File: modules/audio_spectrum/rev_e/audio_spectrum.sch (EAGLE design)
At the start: 109 parts, among them J1 AUDIO-JACK-VERTICAL, J2 MODULE_GENERIC_DEBUG, J3 TC2030-JLINK-L, P1 4k-200k, P2 4k-200k, Q1 NX3008PBK, Q2 NX3008PBK, U1 AT45DB641EUDFN, U10 TLV62130, U2 MP23AB02B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

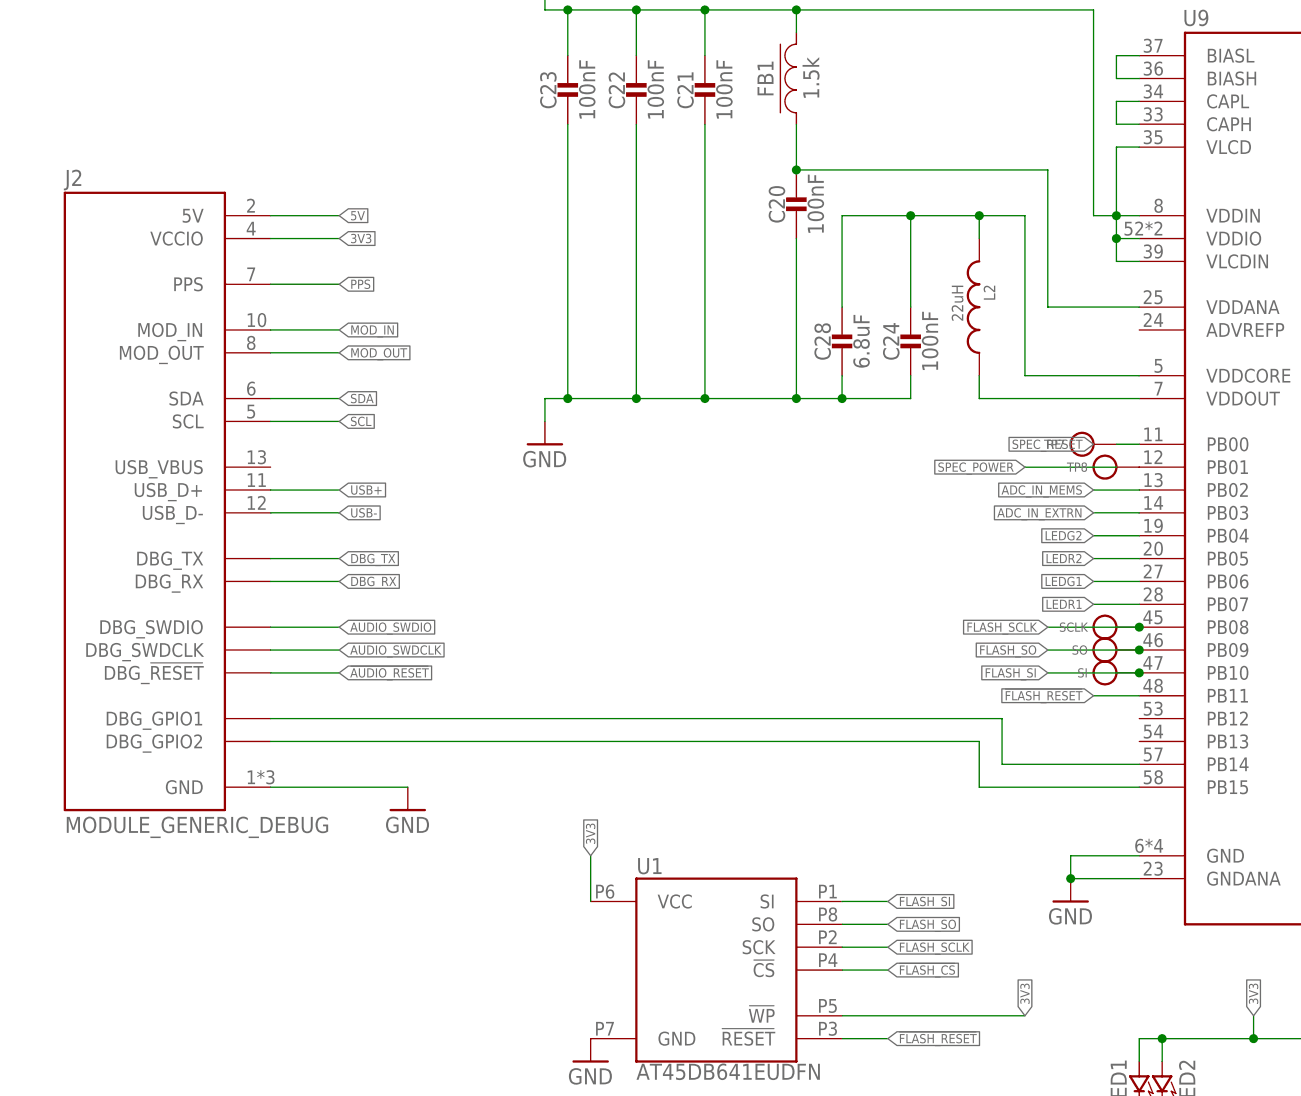
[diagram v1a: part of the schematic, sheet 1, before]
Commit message: changed to design block for header parts
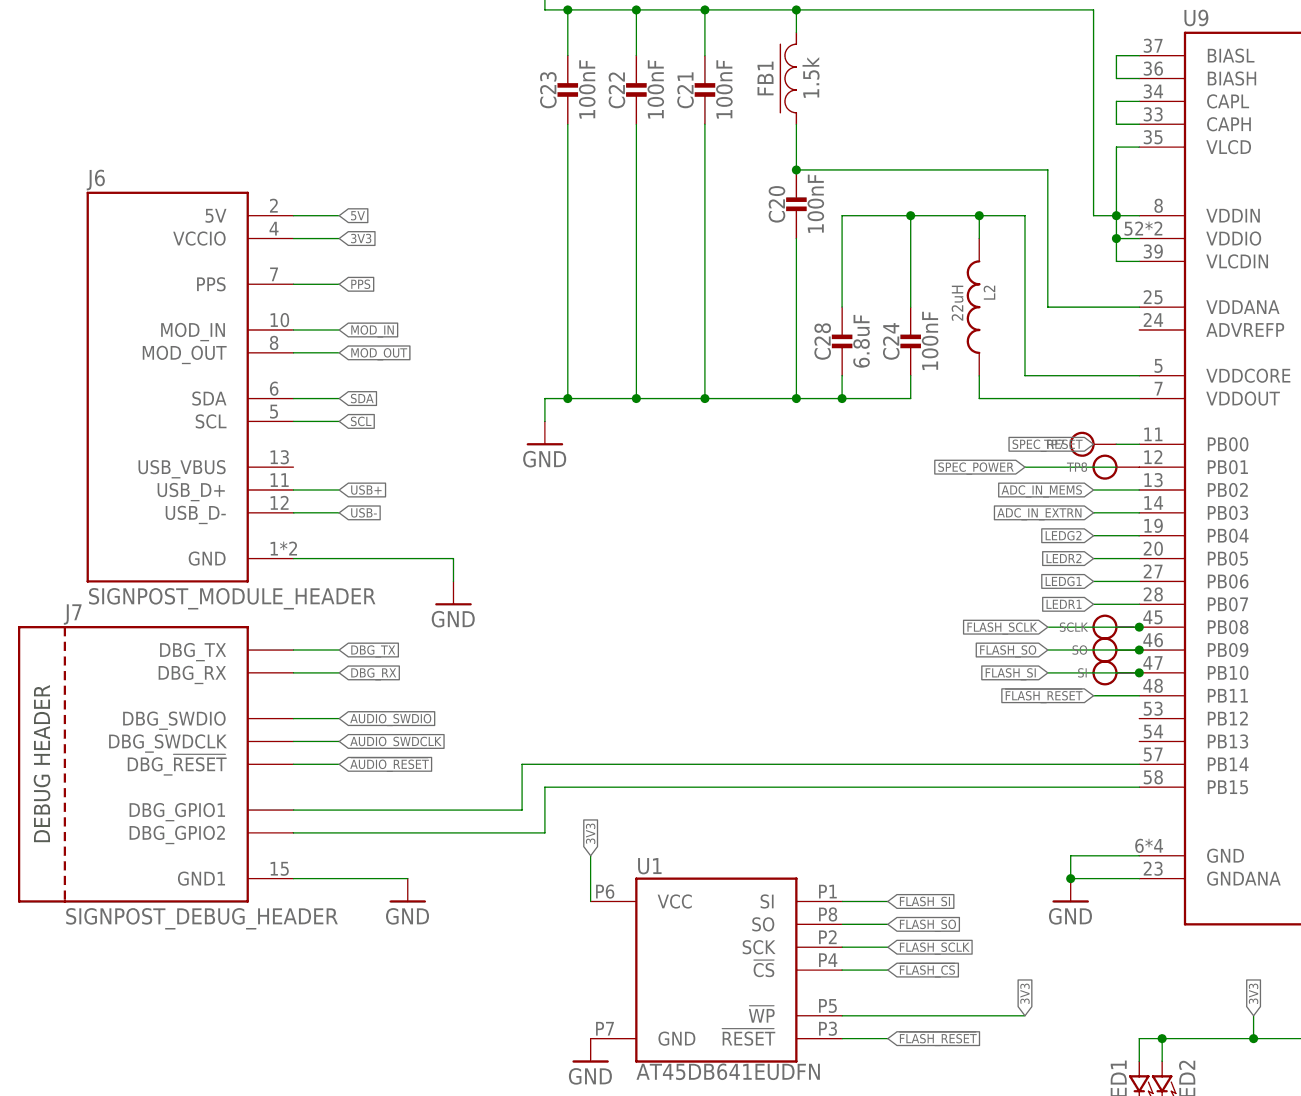
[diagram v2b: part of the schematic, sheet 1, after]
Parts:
- removed J2: MODULE_GENERIC_DEBUG, signpost:MODULE_GENERIC_DEBUG
- added J6: SIGNPOST_MODULE_HEADER, signpost:SIGNPOST_MODULE_HEADER
- added J7: SIGNPOST_DEBUG_HEADER, signpost:SIGNPOST_DEBUG_HEADER
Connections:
- net !AUDIO_RESET: now also J7.DBG_!RESET; no longer J2.DBG_!RESET
- net 3V3: now also J6.VCCIO; no longer J2.VCCIO
- net 5V: now also J6.5V; no longer J2.5V
- net AUDIO_SWDCLK: now also J7.DBG_SWDCLK; no longer J2.DBG_SWDCLK
- net AUDIO_SWDIO: now also J7.DBG_SWDIO; no longer J2.DBG_SWDIO
- net DBG_GPIO1: now also J7.DBG_GPIO1; no longer J2.DBG_GPIO1
- net DBG_GPIO2: now also J7.DBG_GPIO2; no longer J2.DBG_GPIO2
- net DBG_RX: now also J7.DBG_RX; no longer J2.DBG_RX
- net DBG_TX: now also J7.DBG_TX; no longer J2.DBG_TX
- net GND: now also J6.GND, J7.GND1; no longer J2.GND
- net MOD_IN: now also J6.MOD_IN; no longer J2.MOD_IN
- net MOD_OUT: now also J6.MOD_OUT; no longer J2.MOD_OUT
- net PPS: now also J6.PPS; no longer J2.PPS
- net SCL: now also J6.SCL; no longer J2.SCL
- net SDA: now also J6.SDA; no longer J2.SDA
- net USB+: now also J6.USB_D+; no longer J2.USB_D+
- net USB-: now also J6.USB_D-; no longer J2.USB_D-
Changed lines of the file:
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@@
 <?xml version="1.0" encoding="utf-8"?>
 <!DOCTYPE eagle SYSTEM "eagle.dtd">
-<eagle version="8.2.2">
+<eagle version="8.3.1">
 <drawing>
 <settings>
 <setting alwaysvectorfont="no"/>
+<setting keepoldvectorfont="yes"/>
 <setting verticaltext="up"/>
 </settings>
@@
 <attribute name="DIGIKEY" value="445-7484-1-ND"/>
 </part>
-<part name="J2" library="signpost" deviceset="MODULE_GENERIC_DEBUG" device=""/>
 <part name="FRAME2" library="lab11-frames" deviceset="LETTER_L_UMICH" device=""/>
 <part name="U3" library="chips" deviceset="MSGEQ7" device=""/>
@@
 <part name="SI" library="headers" deviceset="TEST_POINT_0.040IN" device=""/>
 <part name="!CS" library="headers" deviceset="TEST_POINT_0.040IN" device=""/>
+<part name="J6" library="signpost" deviceset="SIGNPOST_MODULE_HEADER" device=""/>
+<part name="J7" library="signpost" deviceset="SIGNPOST_DEBUG_HEADER" device=""/>
+<part name="GND28" library="umich" deviceset="GND" device=""/>
 </parts>
 <sheets>
@@
 <attribute name="DIGIKEY" x="96.52" y="139.7" size="1.27" layer="96" align="bottom-center" display="off"/>
 </instance>
-<instance part="J2" gate="G$1" x="22.86" y="132.08"/>
 <instance part="U10" gate="G$1" x="50.8" y="30.48"/>
 <instance part="C31" gate="G$1" x="15.24" y="35.56">
@@
 </instance>
 <instance part="L1" gate="G$1" x="76.2" y="40.64" rot="R90"/>
-<instance part="GND12" gate="1" x="48.26" y="86.36"/>
+<instance part="GND12" gate="1" x="48.26" y="76.2"/>
 <instance part="R2" gate="G$1" x="129.54" y="43.18" smashed="yes" rot="R90">
 <attribute name="DIGIKEY" x="129.54" y="43.18" size="1.27" layer="96" font="vector" rot="R90" display="off"/>
@@
 <instance part="SI" gate="G$1" x="127" y="101.6"/>
 <instance part="!CS" gate="G$1" x="172.72" y="119.38" rot="R180"/>
+<instance part="J6" gate="G$1" x="22.86" y="132.08"/>
+<instance part="J7" gate="G$1" x="5.08" y="76.2"/>
+<instance part="GND28" gate="1" x="53.34" y="109.22"/>
 </instances>
 <busses>
@@
 </segment>
 <segment>
-<pinref part="J2" gate="G$1" pin="GND"/>
-<wire x1="33.02" y1="88.9" x2="48.26" y2="88.9" width="0.1524" layer="91"/>
 <pinref part="GND12" gate="1" pin="GND"/>
+<pinref part="J7" gate="G$1" pin="GND1"/>
+<wire x1="35.56" y1="78.74" x2="48.26" y2="78.74" width="0.1524" layer="91"/>
 </segment>
 <segment>
@@
 <pinref part="U1" gate="G$1" pin="GND"/>
 </segment>
+<segment>
+<pinref part="J6" gate="G$1" pin="GND"/>
+<pinref part="GND28" gate="1" pin="GND"/>
+<wire x1="35.56" y1="114.3" x2="53.34" y2="114.3" width="0.1524" layer="91"/>
+<wire x1="53.34" y1="114.3" x2="53.34" y2="111.76" width="0.1524" layer="91"/>
+</segment>
 </net>
 <net name="AUDIO_SWDCLK" class="0">
@@
 </segment>
 <segment>
-<pinref part="J2" gate="G$1" pin="DBG_SWDCLK"/>
-<wire x1="33.02" y1="104.14" x2="40.64" y2="104.14" width="0.1524" layer="91"/>
-<label x="40.64" y="104.14" size="1.016" layer="95" xref="yes"/>
+<label x="40.64" y="93.98" size="1.016" layer="95" xref="yes"/>
+<pinref part="J7" gate="G$1" pin="DBG_SWDCLK"/>
+<wire x1="35.56" y1="93.98" x2="40.64" y2="93.98" width="0.1524" layer="91"/>
 </segment>
 </net>
@@
 </segment>
 <segment>
-<pinref part="J2" gate="G$1" pin="DBG_!RESET"/>
-<wire x1="33.02" y1="101.6" x2="40.64" y2="101.6" width="0.1524" layer="91"/>
-<label x="40.64" y="101.6" size="1.016" layer="95" xref="yes"/>
+<label x="40.64" y="91.44" size="1.016" layer="95" xref="yes"/>
+<pinref part="J7" gate="G$1" pin="DBG_!RESET"/>
+<wire x1="35.56" y1="91.44" x2="40.64" y2="91.44" width="0.1524" layer="91"/>
 </segment>
 </net>
@@
 </segment>
 <segment>
-<pinref part="J2" gate="G$1" pin="DBG_SWDIO"/>
-<wire x1="33.02" y1="106.68" x2="40.64" y2="106.68" width="0.1524" layer="91"/>
-<label x="40.64" y="106.68" size="1.016" layer="95" xref="yes"/>
+<label x="40.64" y="96.52" size="1.016" layer="95" xref="yes"/>
+<pinref part="J7" gate="G$1" pin="DBG_SWDIO"/>
+<wire x1="35.56" y1="96.52" x2="40.64" y2="96.52" width="0.1524" layer="91"/>
 </segment>
 </net>
@@
 </segment>
 <segment>
-<pinref part="J2" gate="G$1" pin="VCCIO"/>
-<wire x1="33.02" y1="149.86" x2="40.64" y2="149.86" width="0.1524" layer="91"/>
 <label x="40.64" y="149.86" size="1.016" layer="95" xref="yes"/>
+<pinref part="J6" gate="G$1" pin="VCCIO"/>
+<wire x1="35.56" y1="149.86" x2="40.64" y2="149.86" width="0.1524" layer="91"/>
 </segment>
 <segment>
@@
 </segment>
 <segment>
-<pinref part="J2" gate="G$1" pin="5V"/>
-<wire x1="33.02" y1="152.4" x2="40.64" y2="152.4" width="0.1524" layer="91"/>
 <label x="40.64" y="152.4" size="1.016" layer="95" xref="yes"/>
+<pinref part="J6" gate="G$1" pin="5V"/>
+<wire x1="35.56" y1="152.4" x2="40.64" y2="152.4" width="0.1524" layer="91"/>
 </segment>
 </net>
@@
 <net name="PPS" class="0">
 <segment>
-<pinref part="J2" gate="G$1" pin="PPS"/>
-<wire x1="33.02" y1="144.78" x2="40.64" y2="144.78" width="0.1524" layer="91"/>
 <label x="40.64" y="144.78" size="1.016" layer="95" xref="yes"/>
+<pinref part="J6" gate="G$1" pin="PPS"/>
+<wire x1="35.56" y1="144.78" x2="40.64" y2="144.78" width="0.1524" layer="91"/>
 </segment>
 <segment>
@@
 <net name="MOD_IN" class="0">
 <segment>
-<pinref part="J2" gate="G$1" pin="MOD_IN"/>
-<wire x1="33.02" y1="139.7" x2="40.64" y2="139.7" width="0.1524" layer="91"/>
 <label x="40.64" y="139.7" size="1.016" layer="95" xref="yes"/>
+<pinref part="J6" gate="G$1" pin="MOD_IN"/>
+<wire x1="35.56" y1="139.7" x2="40.64" y2="139.7" width="0.1524" layer="91"/>
 </segment>
 <segment>
@@
 <net name="MOD_OUT" class="0">
 <segment>
-<pinref part="J2" gate="G$1" pin="MOD_OUT"/>
-<wire x1="33.02" y1="137.16" x2="40.64" y2="137.16" width="0.1524" layer="91"/>
 <label x="40.64" y="137.16" size="1.016" layer="95" xref="yes"/>
+<pinref part="J6" gate="G$1" pin="MOD_OUT"/>
+<wire x1="35.56" y1="137.16" x2="40.64" y2="137.16" width="0.1524" layer="91"/>
 </segment>
 <segment>
@@
 <net name="SDA" class="0">
 <segment>
-<pinref part="J2" gate="G$1" pin="SDA"/>
-<wire x1="33.02" y1="132.08" x2="40.64" y2="132.08" width="0.1524" layer="91"/>
 <label x="40.64" y="132.08" size="1.016" layer="95" xref="yes"/>
+<pinref part="J6" gate="G$1" pin="SDA"/>
+<wire x1="35.56" y1="132.08" x2="40.64" y2="132.08" width="0.1524" layer="91"/>
 </segment>
 <segment>
@@
 <net name="SCL" class="0">
 <segment>
-<pinref part="J2" gate="G$1" pin="SCL"/>
-<wire x1="33.02" y1="129.54" x2="40.64" y2="129.54" width="0.1524" layer="91"/>
 <label x="40.64" y="129.54" size="1.016" layer="95" xref="yes"/>
+<pinref part="J6" gate="G$1" pin="SCL"/>
+<wire x1="35.56" y1="129.54" x2="40.64" y2="129.54" width="0.1524" layer="91"/>
 </segment>
 <segment>
@@
 <net name="USB+" class="0">
 <segment>
-<pinref part="J2" gate="G$1" pin="USB_D+"/>
-<wire x1="33.02" y1="121.92" x2="40.64" y2="121.92" width="0.1524" layer="91"/>
 <label x="40.64" y="121.92" size="1.016" layer="95" xref="yes"/>
+<pinref part="J6" gate="G$1" pin="USB_D+"/>
+<wire x1="35.56" y1="121.92" x2="40.64" y2="121.92" width="0.1524" layer="91"/>
 </segment>
 <segment>
@@
 <net name="USB-" class="0">
 <segment>
-<pinref part="J2" gate="G$1" pin="USB_D-"/>
-<wire x1="33.02" y1="119.38" x2="40.64" y2="119.38" width="0.1524" layer="91"/>
 <label x="40.64" y="119.38" size="1.016" layer="95" xref="yes"/>
+<pinref part="J6" gate="G$1" pin="USB_D-"/>
+<wire x1="35.56" y1="119.38" x2="40.64" y2="119.38" width="0.1524" layer="91"/>
 </segment>
 <segment>
@@
 <net name="DBG_GPIO1" class="0">
 <segment>
-<pinref part="J2" gate="G$1" pin="DBG_GPIO1"/>
-<wire x1="33.02" y1="96.52" x2="114.3" y2="96.52" width="0.1524" layer="91"/>
 <pinref part="U9" gate="U1" pin="PB14"/>
-<wire x1="114.3" y1="96.52" x2="114.3" y2="91.44" width="0.1524" layer="91"/>
-<wire x1="114.3" y1="91.44" x2="129.54" y2="91.44" width="0.1524" layer="91"/>
+<wire x1="35.56" y1="86.36" x2="60.96" y2="86.36" width="0.1524" layer="91"/>
+<wire x1="60.96" y1="86.36" x2="60.96" y2="91.44" width="0.1524" layer="91"/>
+<wire x1="60.96" y1="91.44" x2="129.54" y2="91.44" width="0.1524" layer="91"/>
+<pinref part="J7" gate="G$1" pin="DBG_GPIO1"/>
 </segment>
 </net>
 <net name="DBG_GPIO2" class="0">
 <segment>
-<pinref part="J2" gate="G$1" pin="DBG_GPIO2"/>
-<wire x1="33.02" y1="93.98" x2="111.76" y2="93.98" width="0.1524" layer="91"/>
 <pinref part="U9" gate="U1" pin="PB15"/>
-<wire x1="111.76" y1="93.98" x2="111.76" y2="88.9" width="0.1524" layer="91"/>
-<wire x1="111.76" y1="88.9" x2="129.54" y2="88.9" width="0.1524" layer="91"/>
+<wire x1="35.56" y1="83.82" x2="63.5" y2="83.82" width="0.1524" layer="91"/>
+<wire x1="63.5" y1="83.82" x2="63.5" y2="88.9" width="0.1524" layer="91"/>
+<pinref part="J7" gate="G$1" pin="DBG_GPIO2"/>
+<wire x1="63.5" y1="88.9" x2="129.54" y2="88.9" width="0.1524" layer="91"/>
 </segment>
 </net>
@@
 <net name="DBG_TX" class="0">
 <segment>
-<pinref part="J2" gate="G$1" pin="DBG_TX"/>
-<wire x1="33.02" y1="114.3" x2="40.64" y2="114.3" width="0.1524" layer="91"/>
-<label x="40.64" y="114.3" size="1.016" layer="95" xref="yes"/>
+<label x="40.64" y="104.14" size="1.016" layer="95" xref="yes"/>
+<pinref part="J7" gate="G$1" pin="DBG_TX"/>
+<wire x1="35.56" y1="104.14" x2="40.64" y2="104.14" width="0.1524" layer="91"/>
 </segment>
 <segment>
@@
 <net name="DBG_RX" class="0">
 <segment>
-<pinref part="J2" gate="G$1" pin="DBG_RX"/>
-<wire x1="33.02" y1="111.76" x2="40.64" y2="111.76" width="0.1524" layer="91"/>
-<label x="40.64" y="111.76" size="1.016" layer="95" xref="yes"/>
-</segment>
-<segment>
+<label x="40.64" y="101.6" size="1.016" layer="95" xref="yes"/>
+<pinref part="J7" gate="G$1" pin="DBG_RX"/>
+<wire x1="35.56" y1="101.6" x2="40.64" y2="101.6" width="0.1524" layer="91"/>
+</segment>
+<segment>

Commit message: renumbered parts
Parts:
- removed J6: SIGNPOST_MODULE_HEADER, signpost:SIGNPOST_MODULE_HEADER
- added J4: TC2030-JLINK-L, connector:TC2030-JLINK-L
- C20: device passives:CAPACITOR0603_CAP -> passives:CAPACITOR0402_CAP; DIGIKEY 490-1532-1-ND -> 490-10777-1-ND
- C24: device passives:CAPACITOR0402_CAP -> passives:CAPACITOR0603_CAP; DIGIKEY 490-10777-1-ND -> 490-1532-1-ND
- C28: value 6.8uF -> 1uF; DIGIKEY 445-7484-1-ND -> 490-1536-1-ND
- C29: value 4.7uF -> 1uF; DIGIKEY 490-3297-1-ND -> 490-1536-1-ND
- C31: value 10uF -> 4.7uF; DIGIKEY 490-6405-1-ND -> 490-3297-1-ND
- C32: value 22uF -> 6.8uF; DIGIKEY 490-13241-1-ND -> 445-7484-1-ND
- C33: value 1uF -> 10uF; DIGIKEY 490-1536-1-ND -> 490-6405-1-ND
- C34: value 1uF -> 22uF; DIGIKEY 490-1536-1-ND -> 490-13241-1-ND
- J3: value TC2030-JLINK-L -> SIGNPOST_MODULE_HEADER; device connector:TC2030-JLINK-L -> signpost:SIGNPOST_MODULE_HEADER
- R21: value 60k -> 20k; DIGIKEY RHM60.4KCLCT-ND -> RHM20KCGCT-ND
- R22, R23, R24: value 100k -> 20k; DIGIKEY RHM100KCGCT-ND -> RHM20KCGCT-ND
- R25: value 100k -> 60k; DIGIKEY RHM100KCGCT-ND -> RHM60.4KCLCT-ND
- R28, R29: value 200k -> 100k; DIGIKEY RHM200KCFCT-ND -> RHM100KCGCT-ND
- R30: value 240k -> 100k; DIGIKEY RHM240KCFCT-ND -> RHM100KCGCT-ND
- R31: value 750k -> 100k; DIGIKEY RHM750KCFCT-ND -> RHM100KCGCT-ND
- R32, R33: value 20k -> 200k; DIGIKEY RHM20KCGCT-ND -> RHM200KCFCT-ND
- R34: value 20k -> 240k; DIGIKEY RHM20KCGCT-ND -> RHM240KCFCT-ND
- R35: value 20k -> 750k; DIGIKEY RHM20KCGCT-ND -> RHM750KCFCT-ND
- renumbered J7 to J2, LED0 to LED4
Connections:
- net !AUDIO_RESET: now also J4.!RESET; no longer J3.!RESET
- net 3V3: now also C24.1, C34.2, J3.VCCIO, J4.VCC, R26.2, R27.2, R29.2, R35.2; no longer C21.1, C32.2, J3.VCC, J6.VCCIO, R22.2, R23.2, R25.2, R31.2
- net 5V: now also C33.1, J3.5V; no longer C31.1, J6.5V
- net AUDIO_SWDCLK: now also J4.SWDCLK, R27.1; no longer J3.SWDCLK, R23.1
- net AUDIO_SWDIO: now also J4.SWDIO, R26.1; no longer J3.SWDIO, R22.1
- net GND: now also C28.1, C29.1, C32.2, C33.2, J4.GND, R21.2, R24.2, R30.2, R31.2, R34.1; no longer C28.2, C31.2, C32.1, C33.1, J6.GND, R26.2, R27.2, R30.1, R32.2, R35.2
- net MOD_IN: now also J3.MOD_IN; no longer J6.MOD_IN
- net MOD_OUT: now also J3.MOD_OUT; no longer J6.MOD_OUT
- net N$12: now also R25.1; no longer R21.1
- net N$13: now also C30.1; no longer C29.1
- net N$14: now also R28.1; no longer R24.1
- net N$15: now also C31.1; no longer C30.1
- net N$2: now also R32.2; no longer R28.2
- net N$20: now also C31.2; no longer C30.2
- net N$27: now also C28.2, R21.1, R22.2; no longer C33.2, R32.1, R33.2
- net N$28: now also C29.2, R23.2, R24.1; no longer C34.2, R34.2, R35.1
- net N$29: now also C20.1, C32.1; no longer C24.1, C28.1
- net N$32: now also C21.1; no longer C20.1
- net N$36: now also R29.1; no longer R25.1
- net N$37: now also R34.2, R35.1; no longer R30.2, R31.1
- net N$5: now also C30.2; no longer C29.2
- net N$6: now also R33.2; no longer R29.2
- net N87: now also R28.2; no longer R24.2
- net N90: now also R25.2; no longer R21.2
- net PPS: now also J3.PPS; no longer J6.PPS
- net SCL: now also J3.SCL; no longer J6.SCL
- net SDA: now also J3.SDA; no longer J6.SDA
- net SPEC2_GATED: now also R23.1, R32.1; no longer R28.1, R34.1
- net SPEC2_POWER: now also R30.1; no longer R26.1
- net SPEC_GATED: now also R22.1; no longer R29.1
- net SPEC_POWER: now also R31.1; no longer R27.1
- net USB+: now also J3.USB_D+; no longer J6.USB_D+
- net USB-: now also J3.USB_D-; no longer J6.USB_D-
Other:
- moved on the sheet: C20, C21, C22, C23, C24, C29, C30, C32, R21, R24, R28, R32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
